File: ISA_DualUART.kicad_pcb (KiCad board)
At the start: 2 copper layers, 176.5 x 90.2 mm, 74 parts, among them J1 ISA BUS, J10 Parallel Port, J2 ADDR_IRQ, J3 UART1_SEL, J4 UART2_SEL, J6 Serial 2 IDC, J7 Serial 1 DB9, J9 Parport IRQ Select, U1 74LS138, U11 74LS30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

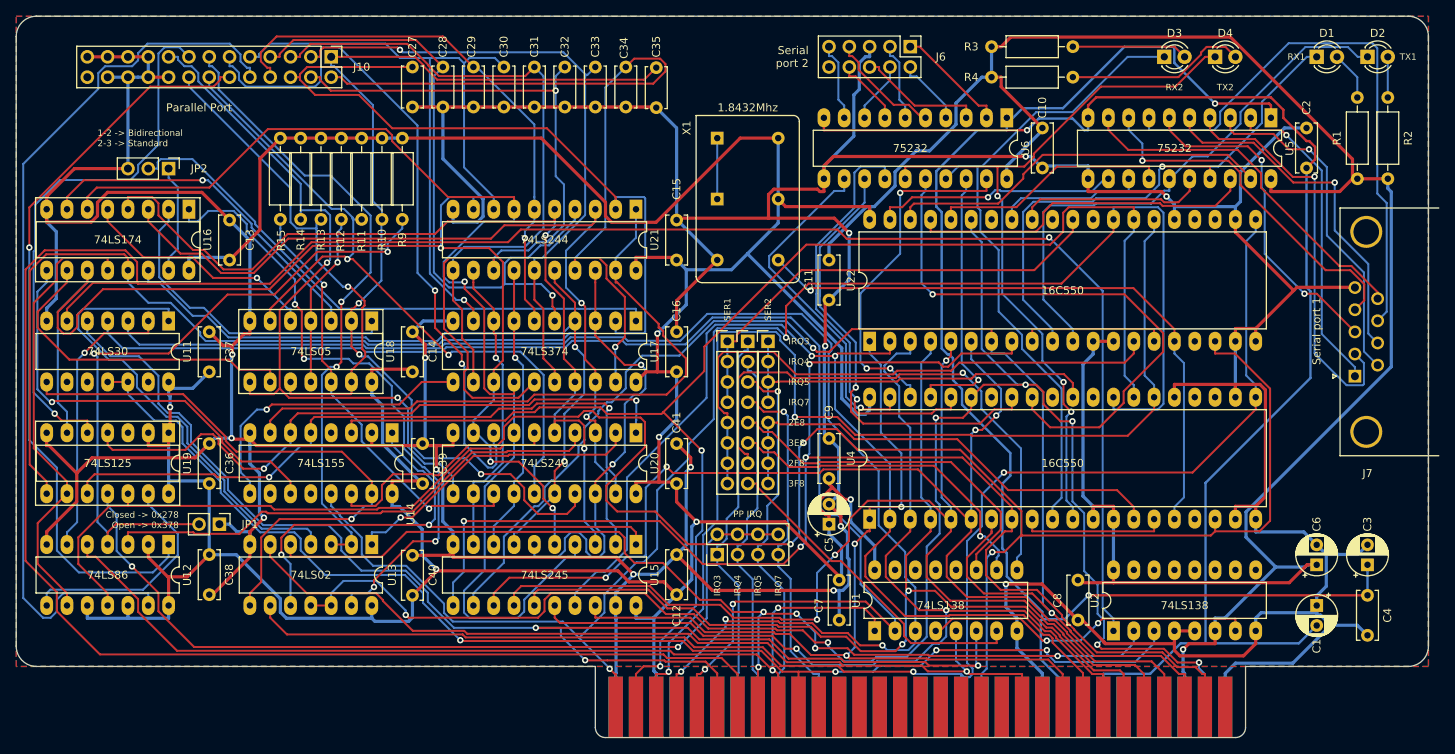
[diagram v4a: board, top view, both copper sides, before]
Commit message: Add text and generate gerbers
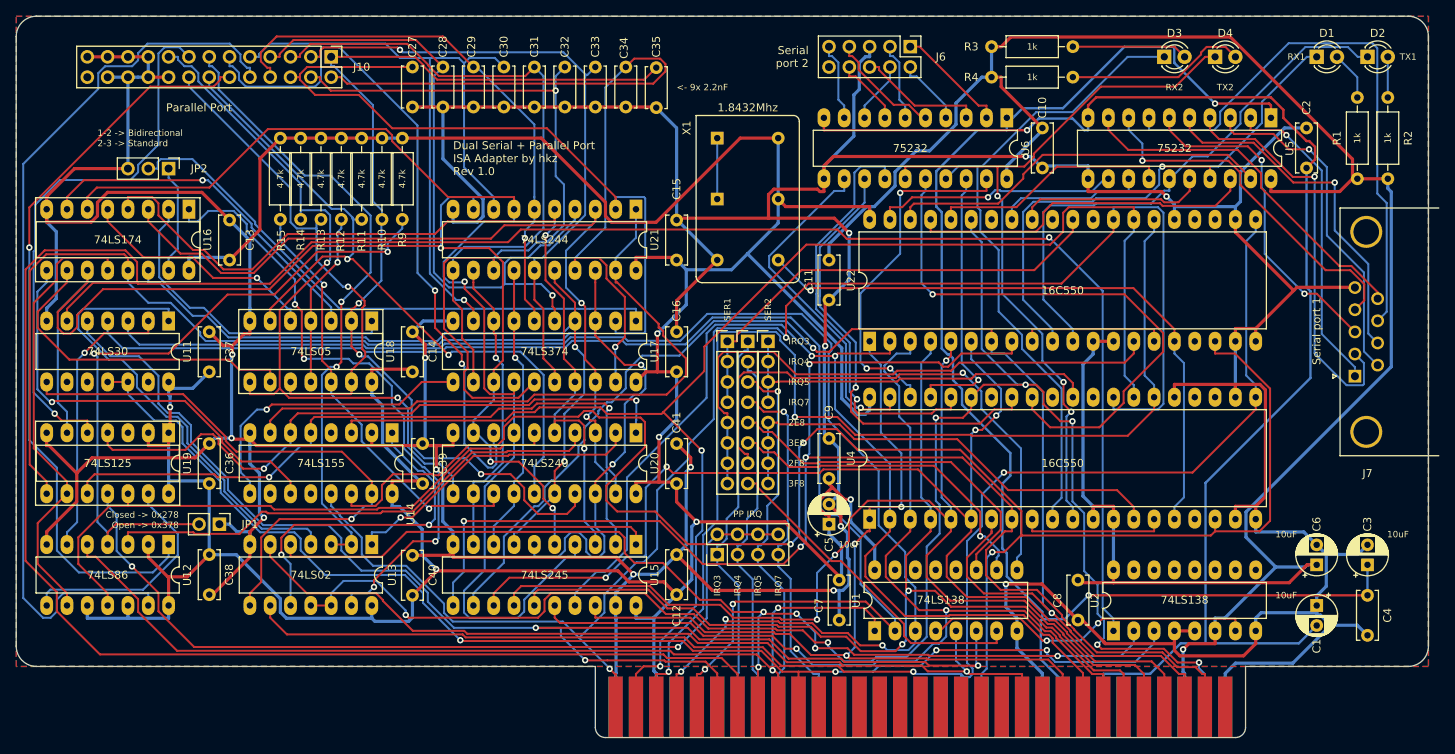
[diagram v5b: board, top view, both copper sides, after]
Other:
- board text added: "10uF"
- board text added: "1k"
- board text added: "4.7k"
- board text added: "<- 9x 2.2nF"
- board text added: "Dual Serial + Parallel Port ISA Adapter by hkz Rev 1.0"
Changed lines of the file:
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@@
   (general
     (thickness 1.6)
-    (drawings 59)
+    (drawings 76)
     (tracks 2964)
     (zones 0)
@@
   (page A3)
   (layers
-    (0 F.Cu signal hide)
-    (31 B.Cu signal hide)
+    (0 F.Cu signal)
+    (31 B.Cu signal)
     (32 B.Adhes user)
     (33 F.Adhes user)
@@
     (pcbplotparams
       (layerselection 0x010fc_ffffffff)
-      (usegerberextensions false)
+      (usegerberextensions true)
       (usegerberattributes true)
       (usegerberadvancedattributes true)
@@
       (outputformat 1)
       (mirror false)
-      (drillshape 1)
+      (drillshape 0)
       (scaleselection 1)
-      (outputdirectory ""))
+      (outputdirectory "gerbers"))
   )
   (net 0 "")
@@
     (add_net /A0)
     (add_net /A1)
+    (add_net /A10)
+    (add_net /A11)
+    (add_net /A12)
+    (add_net /A13)
+    (add_net /A14)
+    (add_net /A15)
+    (add_net /A16)
+    (add_net /A17)
+    (add_net /A18)
+    (add_net /A19)
     (add_net /A2)
     (add_net /A3)
@@
     (add_net /D6)
     (add_net /D7)
+    (add_net /DRQ2)
     (add_net /IRQ3)
     (add_net /IRQ4)
     (add_net /IRQ5)
+    (add_net /IRQ6)
     (add_net /IRQ7)
     (add_net /PARPORT_BD0)
@@
     (add_net /SOUT_1)
     (add_net /SOUT_2)
+    (add_net /TC)
     (add_net /UART1_IRQ)
     (add_net /UART2_IRQ)
     (add_net /~CTS_1)
     (add_net /~CTS_2)
+    (add_net /~DACK2)
     (add_net /~DCD_1)
     (add_net /~DCD_2)
@@
     (add_net /~IOR)
     (add_net /~IOW)
+    (add_net /~MEMR)
+    (add_net /~MEMW)
     (add_net /~PARPORT_ACK)
     (add_net /~PARPORT_AUTOFD)
@@
     (add_net "Net-(D3-Pad2)")
     (add_net "Net-(D4-Pad2)")
+    (add_net "Net-(J1-Pad15)")
+    (add_net "Net-(J1-Pad16)")
+    (add_net "Net-(J1-Pad17)")
+    (add_net "Net-(J1-Pad18)")
+    (add_net "Net-(J1-Pad19)")
+    (add_net "Net-(J1-Pad20)")
+    (add_net "Net-(J1-Pad28)")
+    (add_net "Net-(J1-Pad30)")
+    (add_net "Net-(J1-Pad32)")
+    (add_net "Net-(J1-Pad4)")
+    (add_net "Net-(J1-Pad41)")
+    (add_net "Net-(J1-Pad5)")
+    (add_net "Net-(J1-Pad8)")
+    (add_net "Net-(J10-Pad26)")
+    (add_net "Net-(J6-Pad10)")
     (add_net "Net-(J9-Pad2)")
     (add_net "Net-(JP1-Pad2)")
@@
     (add_net "Net-(R12-Pad2)")
     (add_net "Net-(R15-Pad2)")
+    (add_net "Net-(U1-Pad12)")
+    (add_net "Net-(U1-Pad13)")
+    (add_net "Net-(U1-Pad14)")
+    (add_net "Net-(U1-Pad15)")
     (add_net "Net-(U1-Pad4)")
     (add_net "Net-(U11-Pad1)")
@@
     (add_net "Net-(U12-Pad3)")
     (add_net "Net-(U13-Pad1)")
+    (add_net "Net-(U14-Pad10)")
+    (add_net "Net-(U14-Pad12)")
+    (add_net "Net-(U14-Pad4)")
     (add_net "Net-(U16-Pad10)")
     (add_net "Net-(U16-Pad2)")
     (add_net "Net-(U16-Pad5)")
     (add_net "Net-(U16-Pad7)")
+    (add_net "Net-(U19-Pad3)")
+    (add_net "Net-(U2-Pad10)")
+    (add_net "Net-(U2-Pad11)")
+    (add_net "Net-(U2-Pad12)")
+    (add_net "Net-(U2-Pad13)")
+    (add_net "Net-(U2-Pad14)")
+    (add_net "Net-(U2-Pad15)")
+    (add_net "Net-(U2-Pad9)")
     (add_net "Net-(U22-Pad15)")
+    (add_net "Net-(U22-Pad17)")
+    (add_net "Net-(U22-Pad23)")
+    (add_net "Net-(U22-Pad24)")
+    (add_net "Net-(U22-Pad29)")
+    (add_net "Net-(U22-Pad31)")
+    (add_net "Net-(U22-Pad34)")
     (add_net "Net-(U4-Pad15)")
+    (add_net "Net-(U4-Pad17)")
+    (add_net "Net-(U4-Pad23)")
+    (add_net "Net-(U4-Pad24)")
+    (add_net "Net-(U4-Pad29)")
+    (add_net "Net-(U4-Pad31)")
+    (add_net "Net-(U4-Pad34)")
     (add_net "Net-(X1-Pad1)")
   )
@@
     )
   )
+  (gr_text 10uF (at 297.18 185.42) (layer F.SilkS)
+    (effects (font (size 0.8 0.8) (thickness 0.15)))
+  )
+  (gr_text 10uF (at 311.15 177.8) (layer F.SilkS)
+    (effects (font (size 0.8 0.8) (thickness 0.15)))
+  )
+  (gr_text 10uF (at 297.18 177.8) (layer F.SilkS)
+    (effects (font (size 0.8 0.8) (thickness 0.15)))
+  )
+  (gr_text 10uF (at 242.57 179.07) (layer F.SilkS)
+    (effects (font (size 0.8 0.8) (thickness 0.15)))
+  )
+  (gr_text "Dual Serial + Parallel Port\nISA Adapter by hkz\nRev 1.0" (at 193.04 130.81) (layer F.SilkS)
+    (effects (font (size 1 1) (thickness 0.15)) (justify left))
+  )
+  (gr_text 4.7k (at 186.69 133.35 90) (layer F.SilkS)
+    (effects (font (size 0.8 0.8) (thickness 0.15)))
+  )
+  (gr_text 4.7k (at 184.15 133.35 90) (layer F.SilkS)
+    (effects (font (size 0.8 0.8) (thickness 0.15)))
+  )
+  (gr_text 4.7k (at 181.61 133.35 90) (layer F.SilkS)
+    (effects (font (size 0.8 0.8) (thickness 0.15)))
+  )
+  (gr_text 4.7k (at 179.07 133.35 90) (layer F.SilkS)
+    (effects (font (size 0.8 0.8) (thickness 0.15)))
+  )
+  (gr_text 4.7k (at 176.53 133.35 90) (layer F.SilkS)
+    (effects (font (size 0.8 0.8) (thickness 0.15)))
+  )
+  (gr_text 4.7k (at 173.99 133.35 90) (layer F.SilkS)
+    (effects (font (size 0.8 0.8) (thickness 0.15)))
+  )
+  (gr_text 4.7k (at 171.45 133.35 90) (layer F.SilkS)
+    (effects (font (size 0.8 0.8) (thickness 0.15)))
+  )
+  (gr_text "<- 9x 2.2nF" (at 220.98 121.92) (layer F.SilkS)
+    (effects (font (size 0.8 0.8) (thickness 0.15)) (justify left))
+  )
+  (gr_text 1k (at 306.07 128.27 90) (layer F.SilkS)
+    (effects (font (size 0.8 0.8) (thickness 0.15)))
+  )
+  (gr_text 1k (at 265.43 120.65) (layer F.SilkS)
+    (effects (font (size 0.8 0.8) (thickness 0.15)))
+  )
+  (gr_text 1k (at 265.43 116.84) (layer F.SilkS)
+    (effects (font (size 0.8 0.8) (thickness 0.15)))
+  )
+  (gr_text 1k (at 309.88 128.27 90) (layer F.SilkS)
+    (effects (font (size 0.8 0.8) (thickness 0.15)))
+  )
   (gr_text 1.8432Mhz (at 229.87 124.46) (layer F.SilkS)
     (effects (font (size 1 1) (thickness 0.15)))
@@
     (effects (font (size 1 1) (thickness 0.15)))
   )
-  (gr_text 74LS138 (at 284.48 186.69) (layer F.SilkS)
+  (gr_text 74LS138 (at 284.48 186) (layer F.SilkS)
     (effects (font (size 1 1) (thickness 0.15)))
   )
-  (gr_text 74LS138 (at 254 186.69) (layer F.SilkS)
+  (gr_text 74LS138 (at 254 186) (layer F.SilkS)
     (effects (font (size 1 1) (thickness 0.15)))
   )

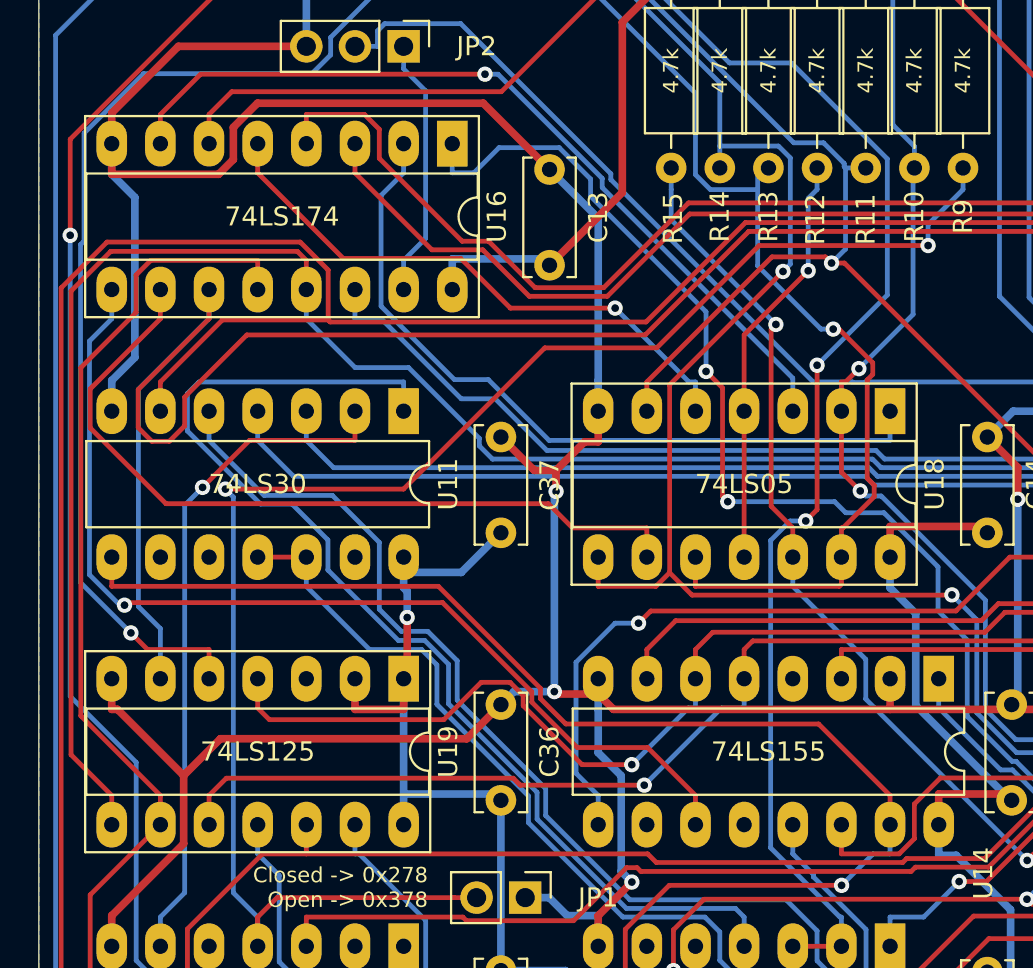
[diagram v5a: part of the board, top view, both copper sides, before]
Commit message: Change socket footprint to normal DIP
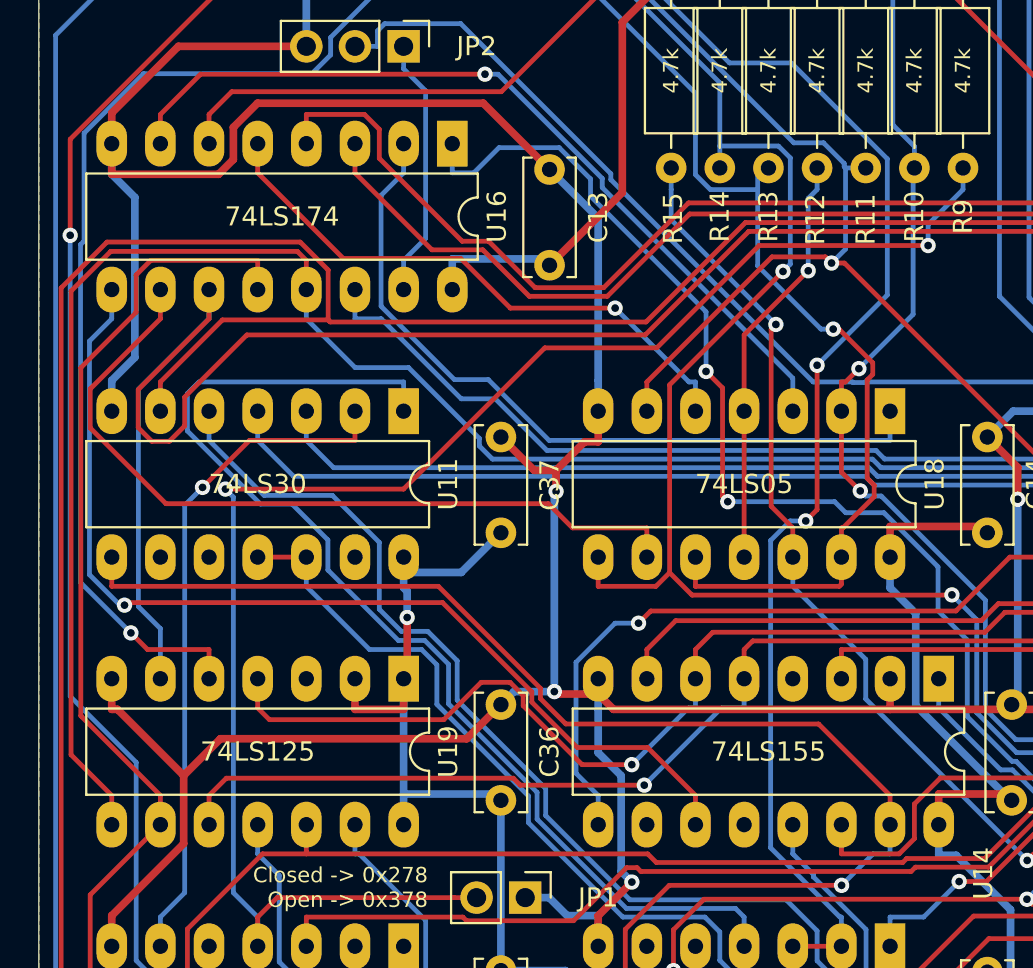
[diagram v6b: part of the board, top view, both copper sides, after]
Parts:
- U16: footprint Package_DIP:DIP-16_W7.62mm_Socket_LongPads -> Package_DIP:DIP-16_W7.62mm_LongPads
- U18, U19: footprint Package_DIP:DIP-14_W7.62mm_Socket_LongPads -> Package_DIP:DIP-14_W7.62mm_LongPads

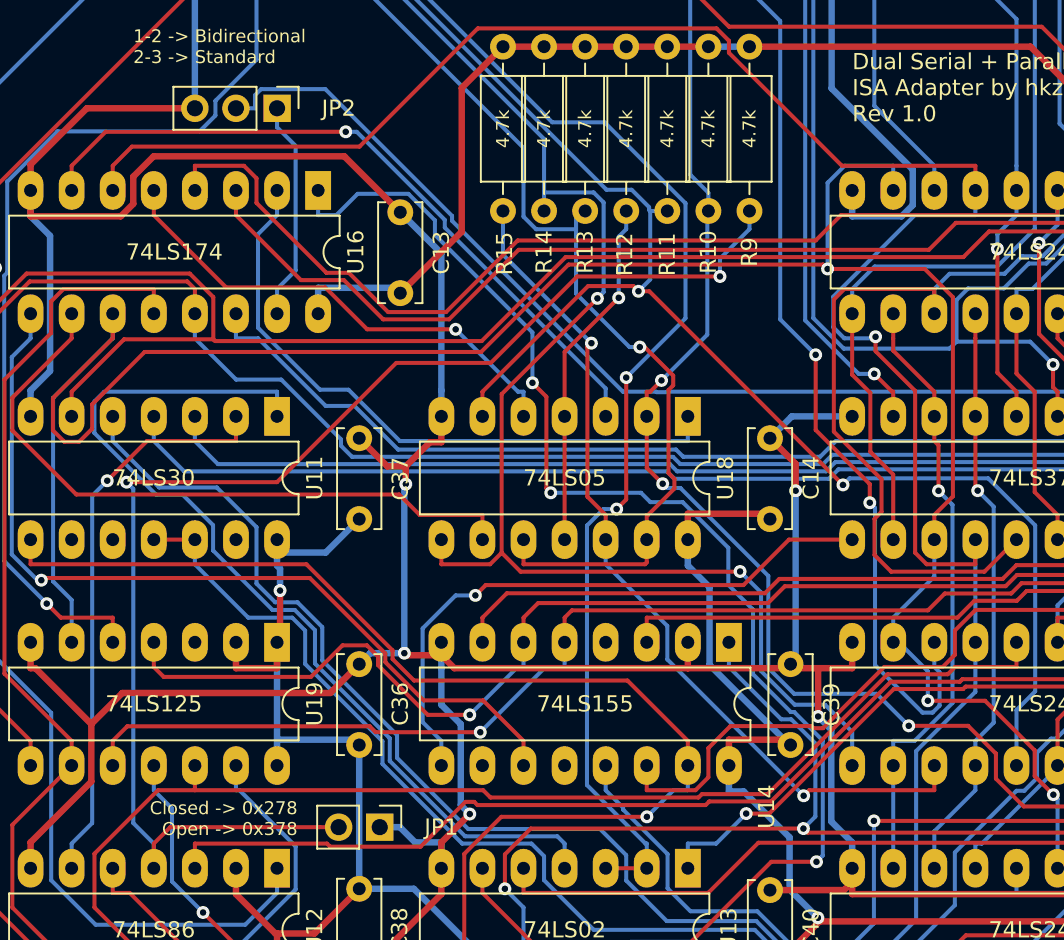
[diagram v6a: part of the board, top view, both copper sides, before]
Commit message: Fix silkscreen
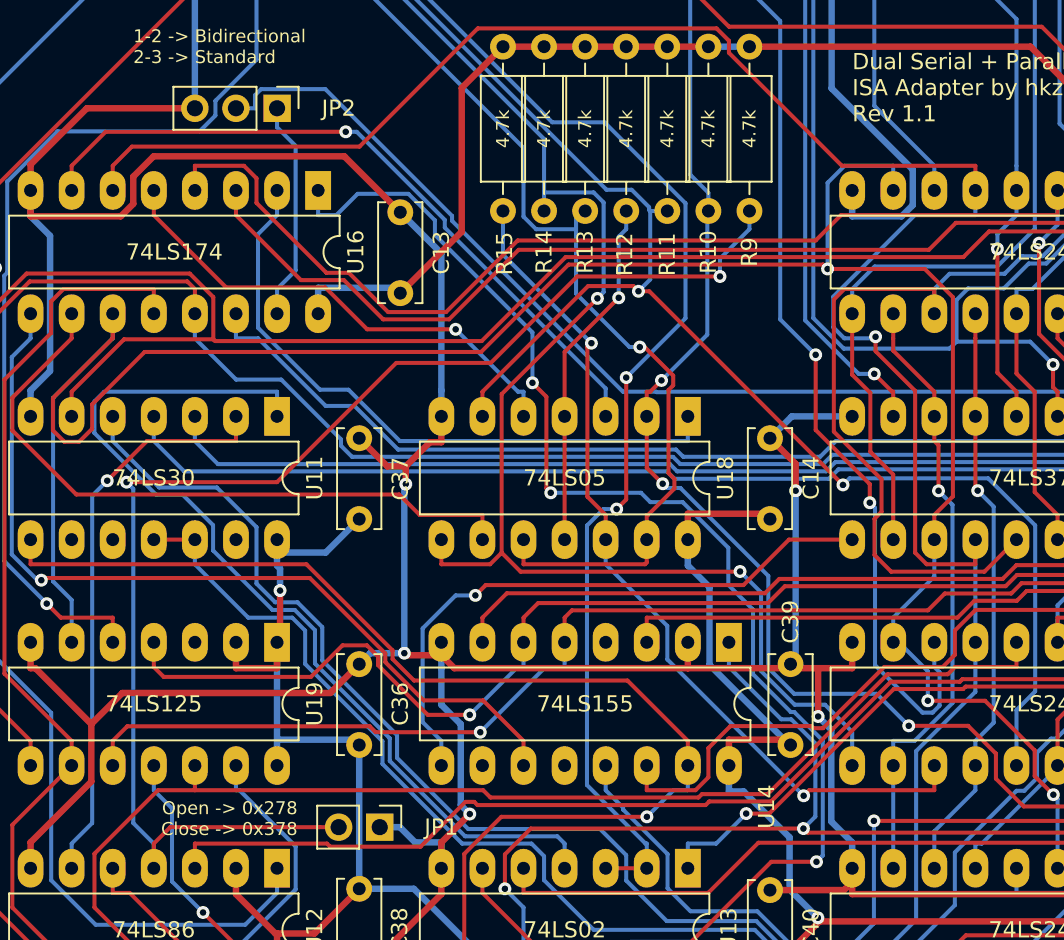
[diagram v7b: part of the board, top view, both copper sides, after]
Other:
- board text added: "Dual Serial + Parallel Port ISA Adapter by hkz Rev 1.1"
- board text added: "Open -> 0x278 Close -> 0x378"
- board text removed: "Closed -> 0x278 Open -> 0x378"
- board text removed: "Dual Serial + Parallel Port ISA Adapter by hkz Rev 1.0"
